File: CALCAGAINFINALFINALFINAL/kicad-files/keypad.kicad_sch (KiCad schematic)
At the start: 101 parts, among them SW100 SW_SPST, SW101 SW_SPST, SW102 SW_SPST, SW49 SW_SPST, SW52 SW_SPST, SW55 SW_SPST, SW56 SW_SPST, SW57 SW_SPST, SW58 SW_SPST, SW59 SW_SPST, SW60 SW_SPST, SW61 SW_SPST, SW62 SW_SPST, SW63 SW_SPST, SW64 SW_SPST, SW65 SW_SPST, SW66 SW_SPST, SW67 SW_SPST, SW68 SW_SPST, SW69 SW_SPST, SW70 SW_SPST, SW71 SW_SPST, SW72 SW_SPST, SW73 SW_SPST, SW74 SW_SPST, SW75 SW_SPST, SW76 SW_SPST, SW77 SW_SPST, SW78 SW_SPST, SW79 SW_SPST, SW80 SW_SPST, SW81 SW_SPST, SW82 SW_SPST, SW83 SW_SPST, SW84 SW_SPST, SW85 SW_SPST, SW86 SW_SPST, SW87 SW_SPST, SW88 SW_SPST, SW89 SW_SPST, SW90 SW_SPST, SW91 SW_SPST, SW92 SW_SPST, SW93 SW_SPST, SW94 SW_SPST, SW95 SW_SPST, SW96 SW_SPST, SW97 SW_SPST, SW98 SW_SPST, SW99 SW_SPST, U7 TCA9535DBR

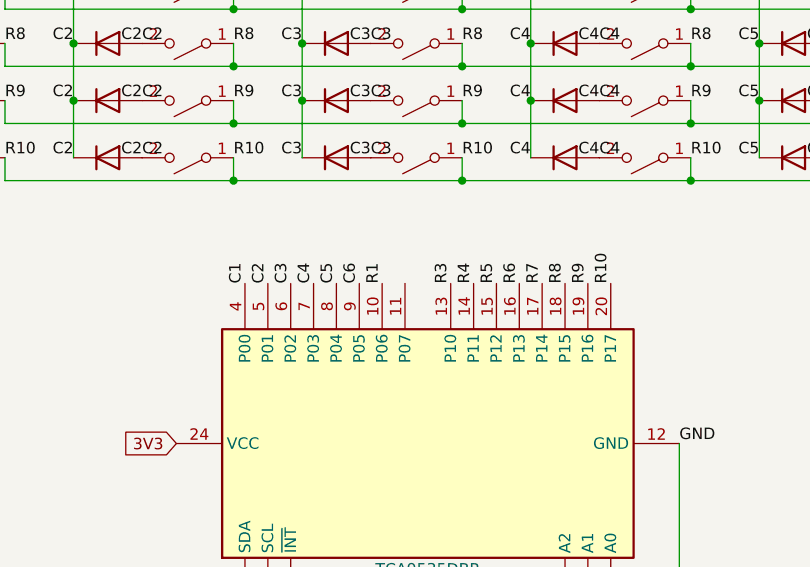
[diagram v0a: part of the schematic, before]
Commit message: added 11pin expansion for accessories and micro-sd card slot
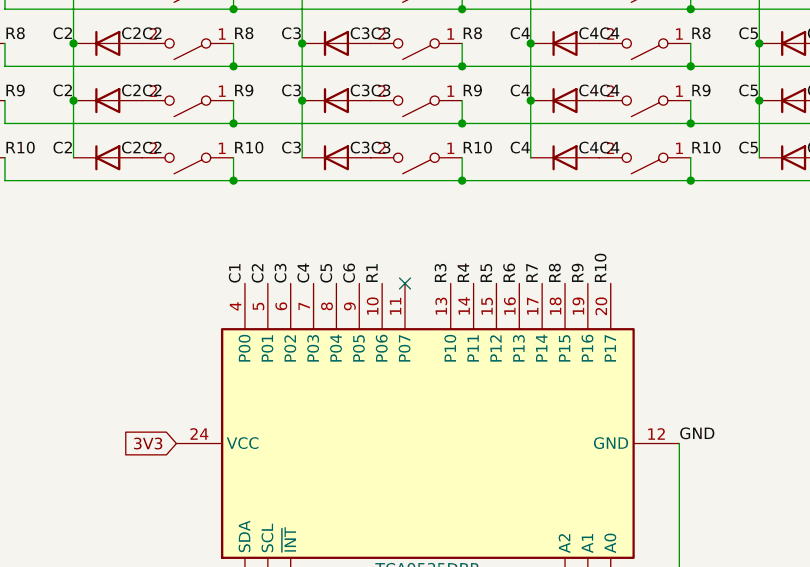
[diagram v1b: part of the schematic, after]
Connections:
- no-connect marks 0 -> 1
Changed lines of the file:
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@@
 		(color 0 0 0 0)
+	)
+	(no_connect
+		(at 134.62 112.014)
 	)
 	(wire

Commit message: nearly finished with the no camera variant schematic stil have 2 drc warnings to fix but should be done in the next few hours.
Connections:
- net R10 is gone; now on net R9: SW61.1 (A), SW70.1 (A), SW79.1 (A), SW88.1 (A), SW97.1 (A), U7.20 (P17)
- net R3: now also SW100.1 (A), SW55.1 (A), SW64.1 (A), SW73.1 (A), SW82.1 (A), SW91.1 (A), U7.14 (P11); no longer SW52.1 (A), SW63.1 (A), SW72.1 (A), SW81.1 (A), SW90.1 (A), SW99.1 (A), U7.13 (P10)
- net R4: now also SW101.1 (A), SW56.1 (A), SW65.1 (A), SW74.1 (A), SW83.1 (A), SW92.1 (A), U7.15 (P12); no longer SW100.1 (A), SW55.1 (A), SW64.1 (A), SW73.1 (A), SW82.1 (A), SW91.1 (A), U7.14 (P11)
- net R5: now also SW102.1 (A), SW57.1 (A), SW66.1 (A), SW75.1 (A), SW84.1 (A), SW93.1 (A), U7.16 (P13); no longer SW101.1 (A), SW56.1 (A), SW65.1 (A), SW74.1 (A), SW83.1 (A), SW92.1 (A), U7.15 (P12)
- net R6: now also SW58.1 (A), SW67.1 (A), SW76.1 (A), SW85.1 (A), SW94.1 (A), U7.17 (P14); no longer SW102.1 (A), SW57.1 (A), SW66.1 (A), SW75.1 (A), SW84.1 (A), SW93.1 (A), U7.16 (P13)
- net R7: now also SW59.1 (A), SW68.1 (A), SW77.1 (A), SW86.1 (A), SW95.1 (A), U7.18 (P15); no longer SW58.1 (A), SW67.1 (A), SW76.1 (A), SW85.1 (A), SW94.1 (A), U7.17 (P14)
- net R8: now also SW60.1 (A), SW69.1 (A), SW78.1 (A), SW87.1 (A), SW96.1 (A), U7.19 (P16); no longer SW59.1 (A), SW68.1 (A), SW77.1 (A), SW86.1 (A), SW95.1 (A), U7.18 (P15)
- net R9: no longer SW60.1 (A), SW69.1 (A), SW78.1 (A), SW87.1 (A), SW96.1 (A), U7.19 (P16)
- new net R2: SW52.1 (A), SW63.1 (A), SW72.1 (A), SW81.1 (A), SW90.1 (A), SW99.1 (A), U7.13 (P10)

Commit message: finalised no-camera branch. designing pcb then committing to origin/no-camera then tracing and adding camera to main
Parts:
- SW100, SW101, SW102, SW49, SW52, SW55, SW56, SW57, SW58, SW59, SW60, SW61, SW62, SW63, SW64, SW65, SW66, SW67, SW68, SW69, SW70, SW71, SW72, SW73, SW74, SW75, SW76, SW77, SW78, SW79, SW80, SW81, SW82, SW83, SW84, SW85, SW86, SW87, SW88, SW89, SW90, SW91, SW92, SW93, SW94, SW95, SW96, SW97, SW98, SW99: footprint (none) -> ButtonPads:conductive pad
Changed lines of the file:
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@@
 			)
 		)
-		(property "Footprint" ""
+		(property "Footprint" "ButtonPads:conductive pad"
 			(at 135.89 98.044 0)
 			(hide yes)
@@
 			)
 		)
-		(property "Footprint" ""
+		(property "Footprint" "ButtonPads:conductive pad"
 			(at 110.49 91.694 0)
 			(hide yes)
@@
 			)
 		)
-		(property "Footprint" ""
+		(property "Footprint" "ButtonPads:conductive pad"
 			(at 212.09 66.294 0)
 			(hide yes)
@@
 			)
 		)
-		(property "Footprint" ""
+		(property "Footprint" "ButtonPads:conductive pad"
 			(at 161.29 78.994 0)
 			(hide yes)
@@
 			)
 		)
-		(property "Footprint" ""
+		(property "Footprint" "ButtonPads:conductive pad"
 			(at 135.89 91.694 0)
 			(hide yes)
@@
 			)
 		)
-		(property "Footprint" ""
+		(property "Footprint" "ButtonPads:conductive pad"
 			(at 161.29 91.694 0)
 			(hide yes)
@@
 			)
 		)
-		(property "Footprint" ""
+		(property "Footprint" "ButtonPads:conductive pad"
 			(at 85.09 53.594 0)
 			(hide yes)
@@
 			)
 		)
-		(property "Footprint" ""
+		(property "Footprint" "ButtonPads:conductive pad"
 			(at 135.89 66.294 0)
 			(hide yes)
@@
 			)
 		)
-		(property "Footprint" ""
+		(property "Footprint" "ButtonPads:conductive pad"
 			(at 186.69 98.044 0)
 			(hide yes)
@@
 			)
 		)
-		(property "Footprint" ""
+		(property "Footprint" "ButtonPads:conductive pad"
 			(at 186.69 45.72 0)
 			(hide yes)
@@
 			)
 		)
-		(property "Footprint" ""
+		(property "Footprint" "ButtonPads:conductive pad"
 			(at 212.09 53.594 0)
 			(hide yes)
@@
 			)
 		)
-		(property "Footprint" ""
+		(property "Footprint" "ButtonPads:conductive pad"
 			(at 135.89 53.594 0)
 			(hide yes)
@@
 			)
 		)
-		(property "Footprint" ""
+		(property "Footprint" "ButtonPads:conductive pad"
 			(at 212.09 45.72 0)
 			(hide yes)
@@
 			)
 		)
-		(property "Footprint" ""
+		(property "Footprint" "ButtonPads:conductive pad"
 			(at 186.69 78.994 0)
 			(hide yes)
@@
 			)
 		)
-		(property "Footprint" ""
+		(property "Footprint" "ButtonPads:conductive pad"
 			(at 110.49 72.644 0)
 			(hide yes)
@@
 			)
 		)
-		(property "Footprint" ""
+		(property "Footprint" "ButtonPads:conductive pad"
 			(at 110.49 98.044 0)
 			(hide yes)
@@
 			)
 		)
-		(property "Footprint" ""
+		(property "Footprint" "ButtonPads:conductive pad"
 			(at 186.69 91.694 0)
 			(hide yes)
@@
 			)
 		)
-		(property "Footprint" ""
+		(property "Footprint" "ButtonPads:conductive pad"
 			(at 110.49 78.994 0)
 			(hide yes)
@@
 			)
 		)
-		(property "Footprint" ""
+		(property "Footprint" "ButtonPads:conductive pad"
 			(at 135.89 78.994 0)
 			(hide yes)
@@
 			)
 		)
-		(property "Footprint" ""
+		(property "Footprint" "ButtonPads:conductive pad"
 			(at 161.29 98.044 0)
 			(hide yes)
@@
 			)
 		)
-		(property "Footprint" ""
+		(property "Footprint" "ButtonPads:conductive pad"
 			(at 110.49 66.294 0)
 			(hide yes)
@@
 			)
 		)
-		(property "Footprint" ""
+		(property "Footprint" "ButtonPads:conductive pad"
 			(at 85.09 72.644 0)
 			(hide yes)
@@
 			)
 		)
-		(property "Footprint" ""
+		(property "Footprint" "ButtonPads:conductive pad"
 			(at 186.69 85.344 0)
 			(hide yes)
@@
 			)
 		)
-		(property "Footprint" ""
+		(property "Footprint" "ButtonPads:conductive pad"
 			(at 110.49 53.594 0)
 			(hide yes)
@@
 			)
 		)
-		(property "Footprint" ""
+		(property "Footprint" "ButtonPads:conductive pad"
 			(at 212.09 59.944 0)
 			(hide yes)
@@
 			)
 		)
-		(property "Footprint" ""
+		(property "Footprint" "ButtonPads:conductive pad"
 			(at 85.09 59.944 0)
 			(hide yes)
@@
 			)
 		)
-		(property "Footprint" ""
+		(property "Footprint" "ButtonPads:conductive pad"
 			(at 161.29 72.644 0)
 			(hide yes)
@@
 			)
 		)
-		(property "Footprint" ""
+		(property "Footprint" "ButtonPads:conductive pad"
 			(at 161.29 53.594 0)
 			(hide yes)
@@
 			)
 		)
-		(property "Footprint" ""
+		(property "Footprint" "ButtonPads:conductive pad"
 			(at 85.09 66.294 0)
 			(hide yes)
@@
 			)
 		)
-		(property "Footprint" ""
+		(property "Footprint" "ButtonPads:conductive pad"
 			(at 135.89 45.72 0)
 			(hide yes)
@@
 			)
 		)
-		(property "Footprint" ""
+		(property "Footprint" "ButtonPads:conductive pad"
 			(at 212.09 72.644 0)
 			(hide yes)
@@
 			)
 		)
-		(property "Footprint" ""
+		(property "Footprint" "ButtonPads:conductive pad"
 			(at 135.89 59.944 0)
 			(hide yes)
@@
 			)
 		)
-		(property "Footprint" ""
+		(property "Footprint" "ButtonPads:conductive pad"
 			(at 85.09 78.994 0)
 			(hide yes)
@@
 			)
 		)
-		(property "Footprint" ""
+		(property "Footprint" "ButtonPads:conductive pad"
 			(at 186.69 66.294 0)
 			(hide yes)
@@
 			)
 		)
-		(property "Footprint" ""
+		(property "Footprint" "ButtonPads:conductive pad"
 			(at 161.29 66.294 0)
 			(hide yes)
@@
 			)
 		)
-		(property "Footprint" ""
+		(property "Footprint" "ButtonPads:conductive pad"
 			(at 85.09 85.344 0)
 			(hide yes)
@@
 			)
 		)
-		(property "Footprint" ""
+		(property "Footprint" "ButtonPads:conductive pad"
 			(at 186.69 53.594 0)
 			(hide yes)
@@
 			)
 		)
-		(property "Footprint" ""
+		(property "Footprint" "ButtonPads:conductive pad"
 			(at 161.29 59.944 0)
 			(hide yes)
@@
 			)
 		)
-		(property "Footprint" ""
+		(property "Footprint" "ButtonPads:conductive pad"
 			(at 110.49 85.344 0)
 			(hide yes)
@@
 			)
 		)
-		(property "Footprint" ""
+		(property "Footprint" "ButtonPads:conductive pad"
 			(at 85.09 91.694 0)
 			(hide yes)
@@
 			)
 		)
-		(property "Footprint" ""
+		(property "Footprint" "ButtonPads:conductive pad"
 			(at 186.69 72.644 0)
 			(hide yes)
@@
 			)
 		)
-		(property "Footprint" ""
+		(property "Footprint" "ButtonPads:conductive pad"
 			(at 161.29 85.344 0)
 			(hide yes)
@@
 			)
 		)
-		(property "Footprint" ""
+		(property "Footprint" "ButtonPads:conductive pad"
 			(at 186.69 59.944 0)
 			(hide yes)
@@
 			)
 		)
-		(property "Footprint" ""
+		(property "Footprint" "ButtonPads:conductive pad"
 			(at 85.09 98.044 0)
 			(hide yes)
@@
 			)
 		)
-		(property "Footprint" ""
+		(property "Footprint" "ButtonPads:conductive pad"
 			(at 135.89 85.344 0)
 			(hide yes)
@@
 			)
 		)
-		(property "Footprint" ""
+		(property "Footprint" "ButtonPads:conductive pad"
 			(at 135.89 72.644 0)
 			(hide yes)
@@
 			)
 		)
-		(property "Footprint" ""
+		(property "Footprint" "ButtonPads:conductive pad"
 			(at 110.49 59.944 0)
 			(hide yes)
@@
 			)
 		)
-		(property "Footprint" ""
+		(property "Footprint" "ButtonPads:conductive pad"
 			(at 161.29 45.466 0)
 			(hide yes)
@@
 			)
 		)
-		(property "Footprint" ""
+		(property "Footprint" "ButtonPads:conductive pad"
 			(at 110.49 45.72 0)
 			(hide yes)
@@
 			)
 		)
-		(property "Footprint" ""
+		(property "Footprint" "ButtonPads:conductive pad"
 			(at 85.09 45.72 0)
 			(hide yes)

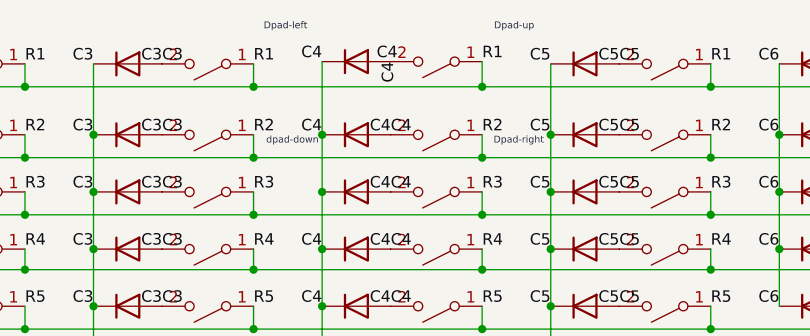
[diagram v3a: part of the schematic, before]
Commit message: finalised pcb w camera. thing is im kinda poor rn and ill prob get enough money to order pcba after 2 weeks. until then ima js focus on school and get thru to working on tweaking the HAL and ui to match my spec and the design language of ABSOLUT-CAS
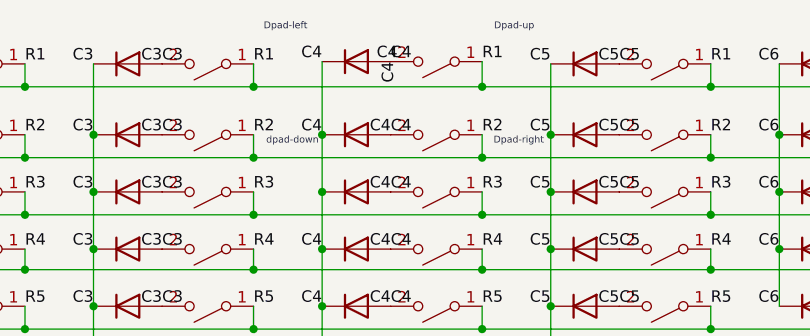
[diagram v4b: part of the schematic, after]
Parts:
- SW100, SW101, SW102, SW49, SW52, SW55, SW56, SW57, SW58, SW59, SW60, SW61, SW62, SW63, SW64, SW65, SW66, SW67, SW68, SW69, SW70, SW71, SW72, SW73, SW74, SW75, SW76, SW77, SW78, SW79, SW80, SW81, SW82, SW83, SW84, SW85, SW86, SW87, SW88, SW89, SW90, SW91, SW92, SW93, SW94, SW95, SW96, SW97, SW98, SW99: now left out of the parts list
- U7: KiLib_Generator (none) -> package/gullwing; LCSC (none) -> C22396388
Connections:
- net C4: now also D82.2 (A), SW80.2 (B)

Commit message: Turns out my whole power thing was absolutely retarded i should REALLY stop relying on gemini its actually retarded as fuh. Ima start js rawdogging it w forums and reddit. once its functional ima order it. i gota remember there no deadline better do it right the first time.
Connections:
- net GND: now also U7.11 (P07)
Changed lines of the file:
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@@
+		)
+	)
+	(label "GND"
+		(at 134.62 112.014 90)
+		(effects
+			(font
+				(size 1.27 1.27)
+			)
+			(justify left bottom)
 		)
 	)

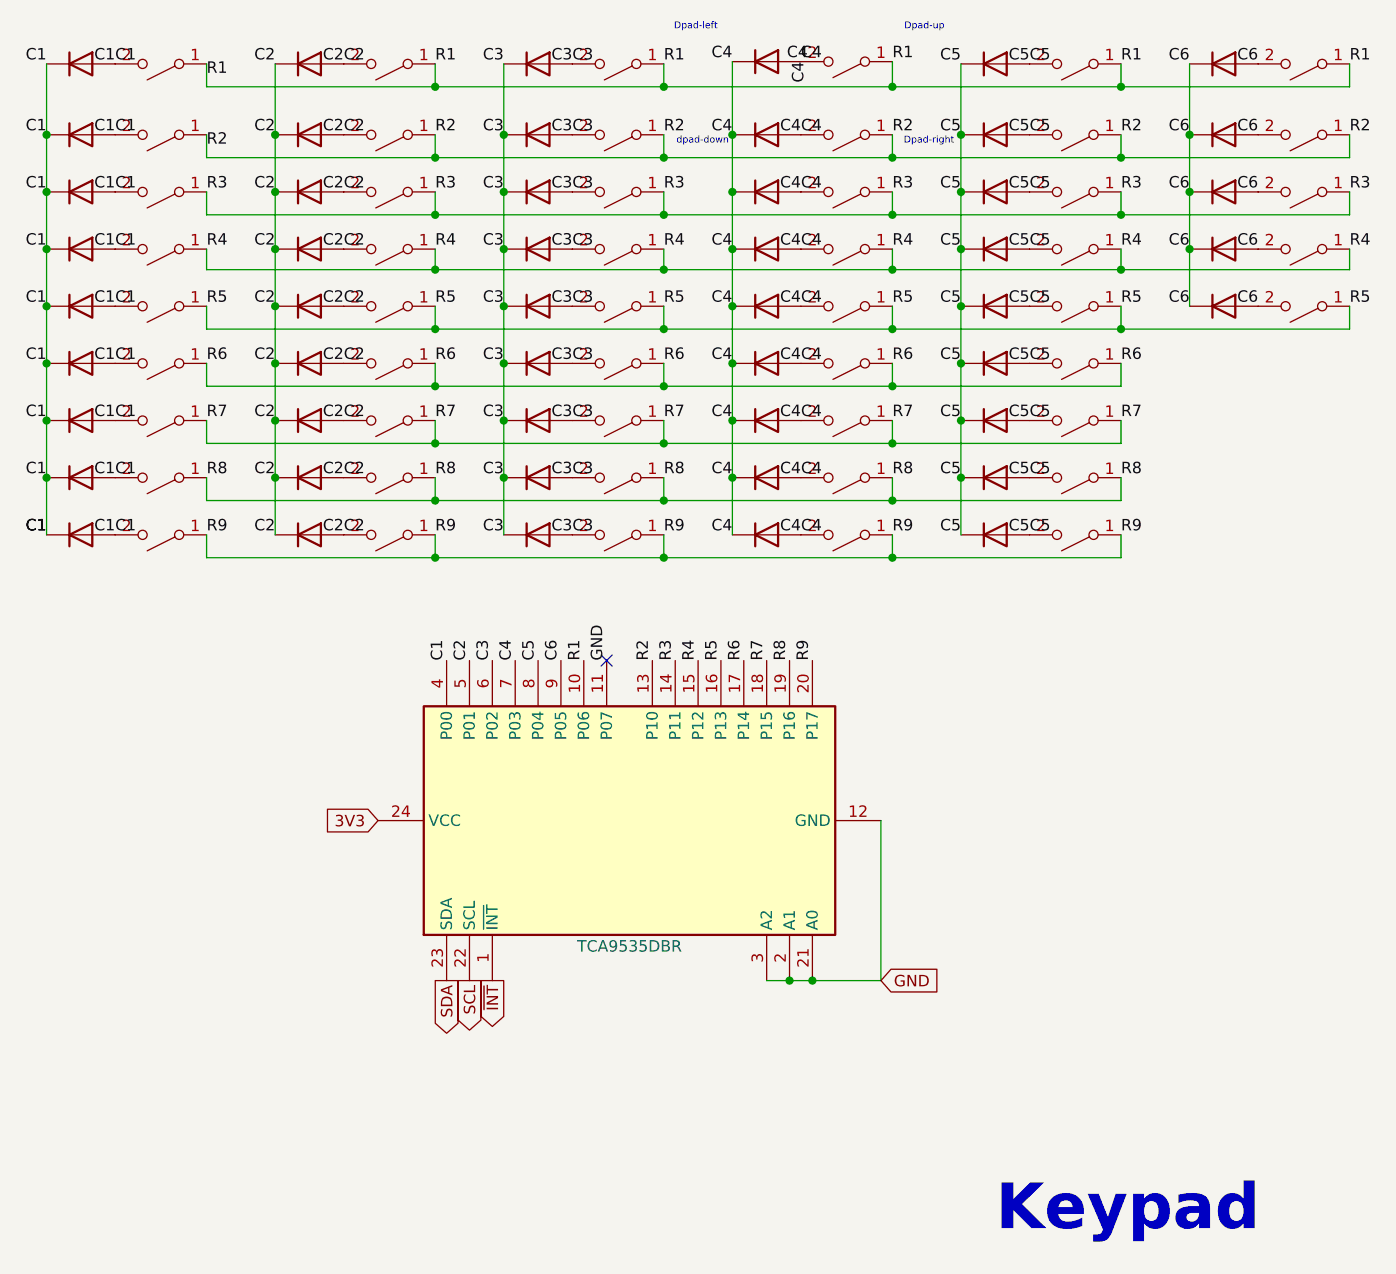
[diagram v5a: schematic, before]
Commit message: workin on matching up the pcb with the schematic gona chuck it on pcbreview then wait till i can stack up enough cash to order the first pcba. i need to make sure the design is 100% otherwise im js spending 300 bucks on a paperweight. so far the logic seems good js need to fix up some clerical errors w schematic.
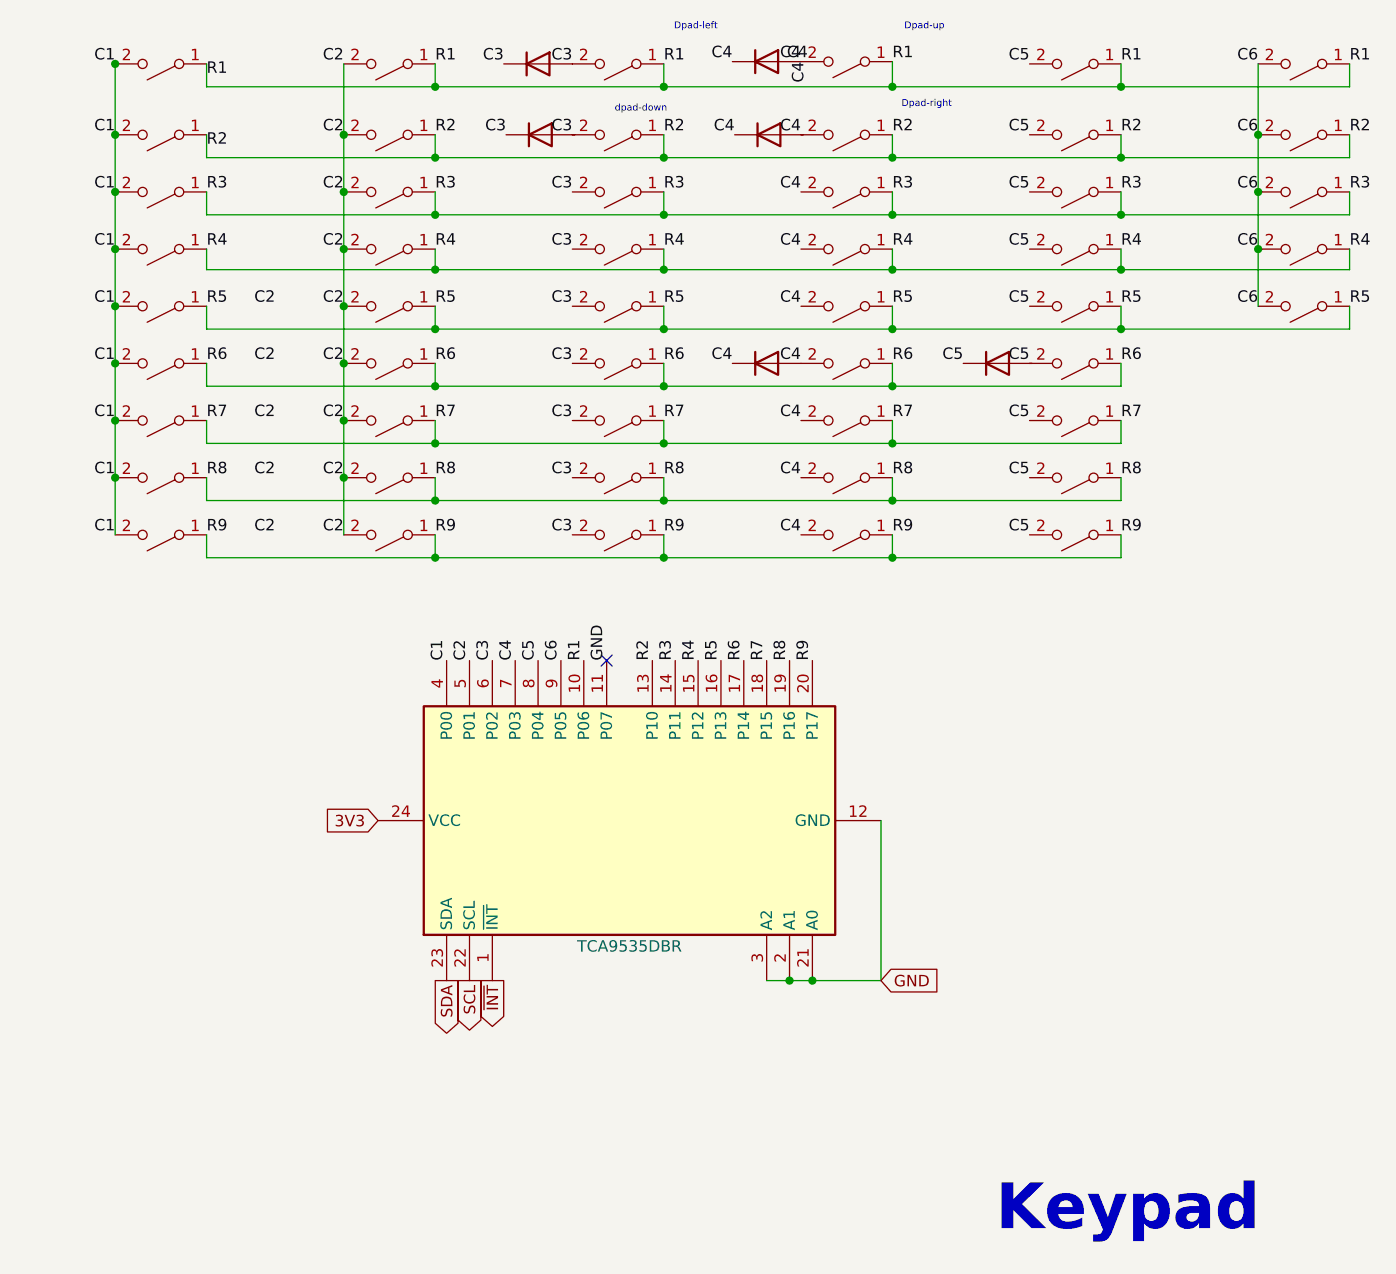
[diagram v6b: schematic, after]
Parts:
- removed D100, D101, D102, D103, D104, D55, D56, D57, D58, D59, D60, D61, D62, D63, D64, D65, D66, D67, D68, D69, D70, D71, D72, D73, D74, D75, D76, D77, D78, D79, D80, D81, D82, D83, D84, D85, D86, D87, D88, D89, D90, D91, D92, D93, D94, D95, D96, D97, D98, D99: 1N4001, Diode_THT:D_DO-41_SOD81_P10.16mm_Horizontal, symbol Diode:1N4001
- added D1, D2, D3, D4, D5, D6: 1N4001, Diode_THT:D_DO-41_SOD81_P10.16mm_Horizontal, symbol Diode:1N4001
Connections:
- net C3: now also D1.1 (K), D1.2 (A), D2.1 (K)
- net C4: now also D3.1 (K), D4.1 (K), D4.2 (A), D6.1 (K), D6.2 (A)
- net C5: now also D5.1 (K)

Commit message: yo chat this actually for reals the order now im ordering it and neva openin kicad again ong
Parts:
- removed D3, D4, D6: 1N4001, Diode_THT:D_DO-41_SOD81_P10.16mm_Horizontal, symbol Diode:1N4001
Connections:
- net C3: no longer D1.1 (K), D1.2 (A), D2.1 (K)
- net C5: no longer D5.1 (K), SW94.2 (B)
- net GND: no longer U7.11 (P07)
- net R1: now also D1.1 (K), D1.2 (A)
- net R2: now also D2.1 (K), D2.2 (A)
- net R6: now also D5.1 (K), D5.2 (A)
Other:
- note added: "AC"
- note added: "DEL"
- note added: "I2C expander"
